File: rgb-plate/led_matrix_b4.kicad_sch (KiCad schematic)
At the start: 32 parts

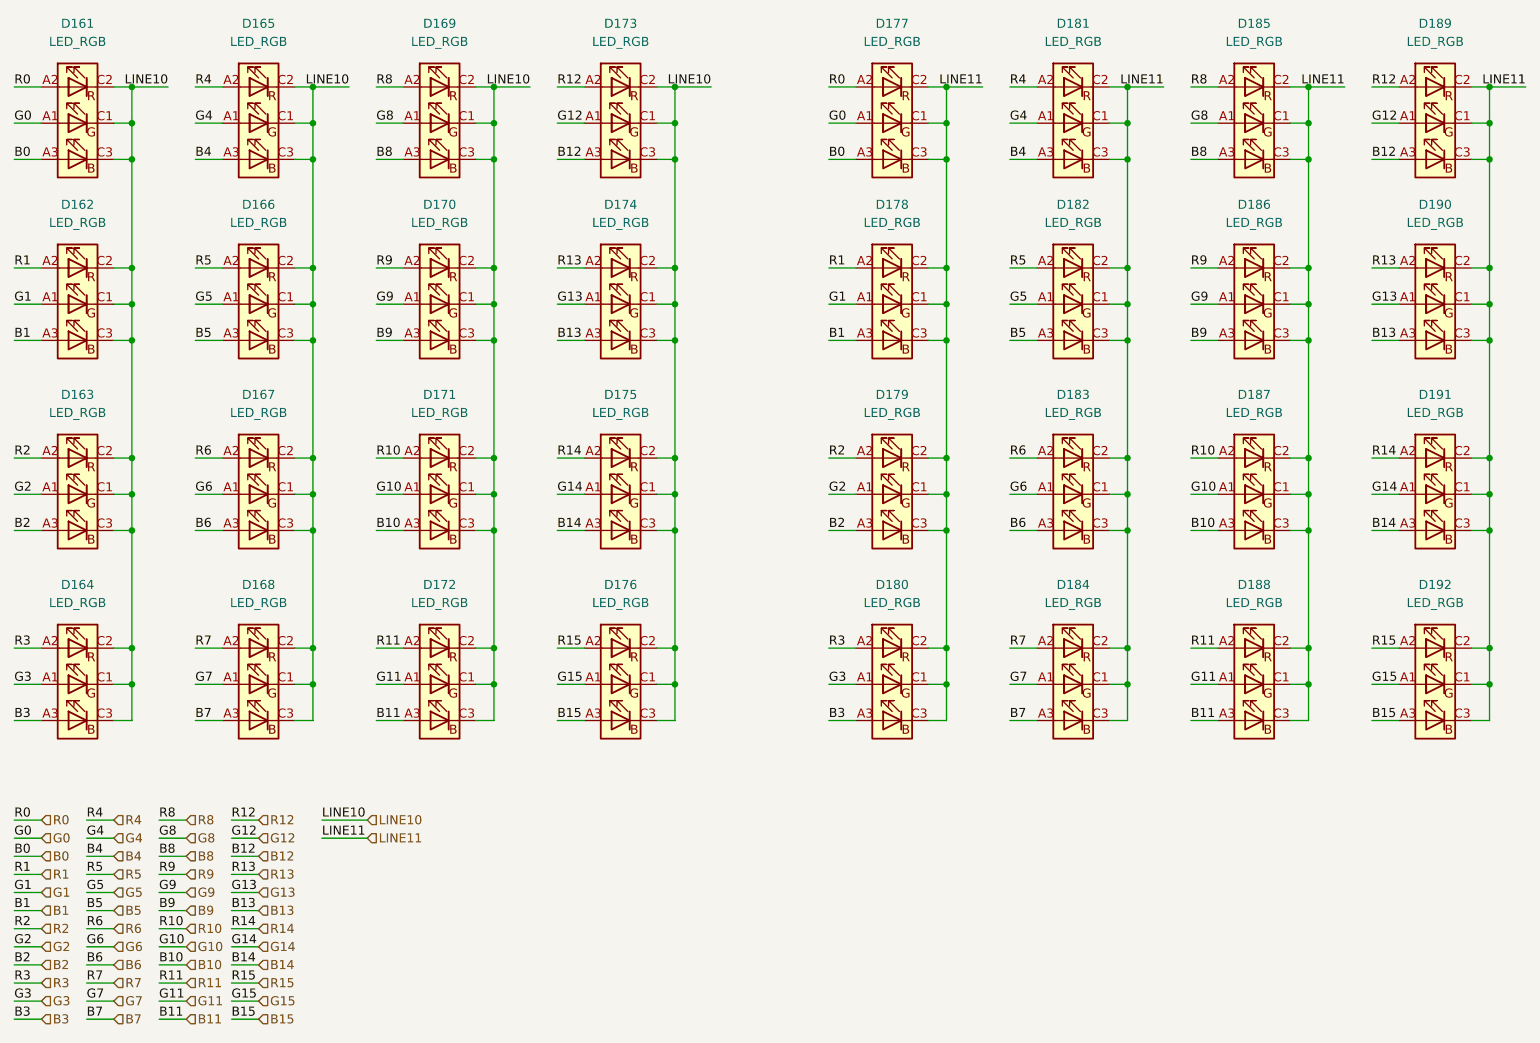
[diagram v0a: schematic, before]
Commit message: initial layout on single board, may need to split up
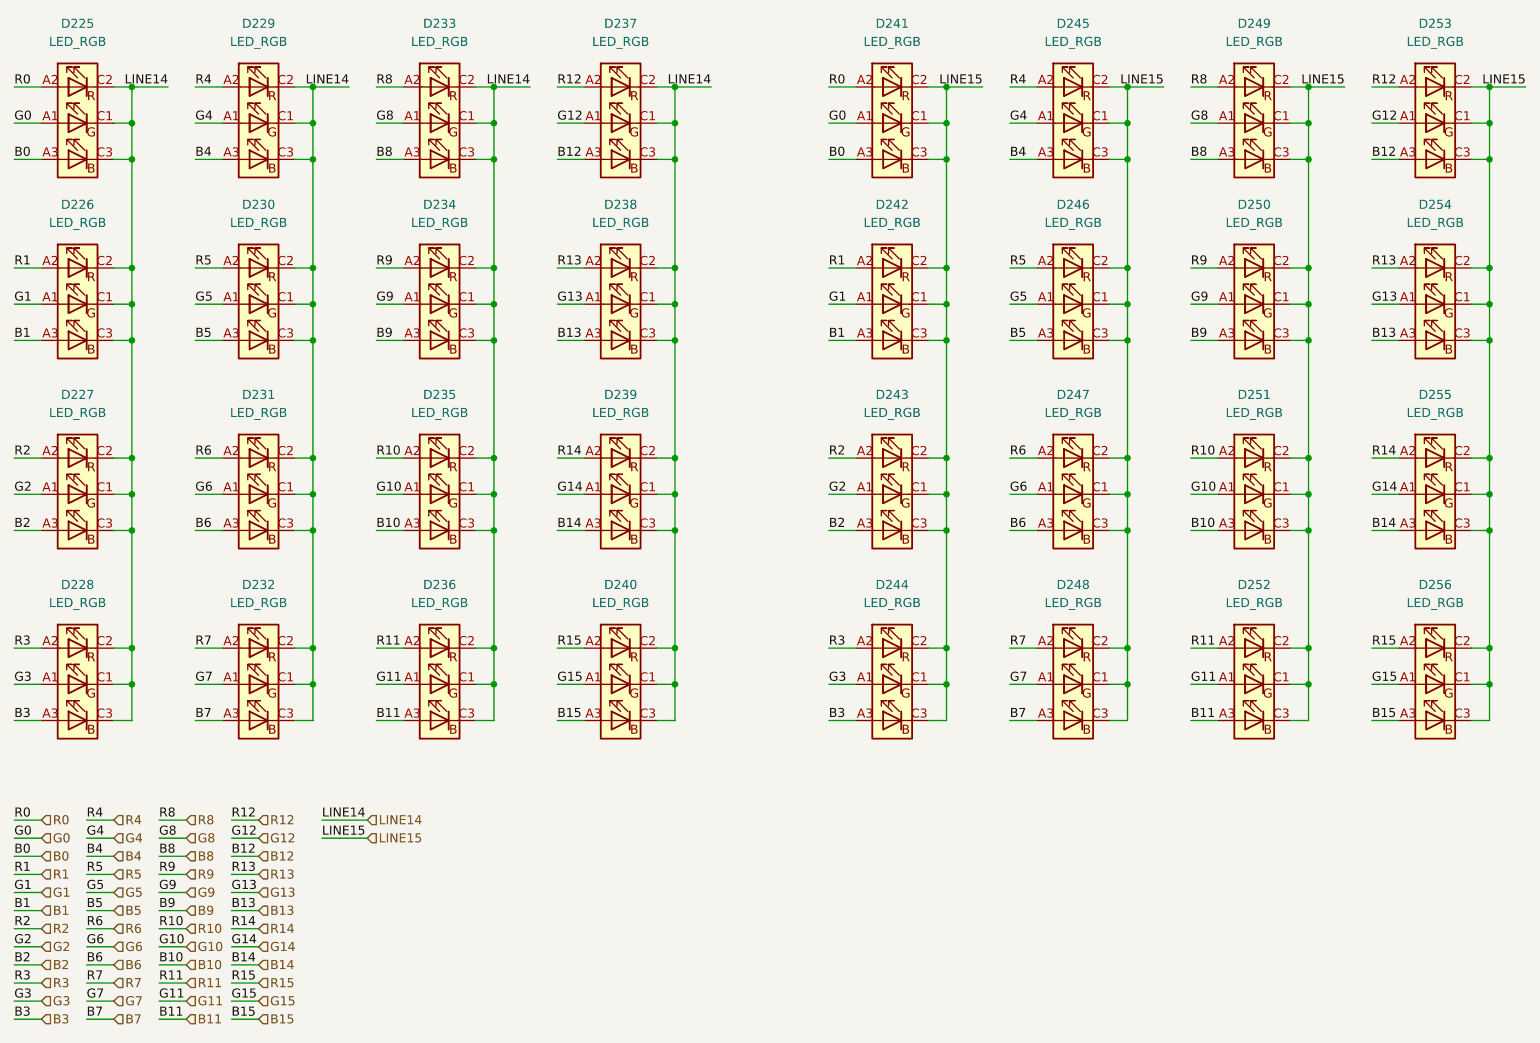
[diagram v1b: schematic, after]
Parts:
- removed D161, D162, D163, D164, D165, D166, D167, D168, D169, D170, D171, D172, D173, D174, D175, D176, D177, D178, D179, D180, D181, D182, D183, D184, D185, D186, D187, D188, D189, D190, D191, D192: LED_RGB, LRTBGVSR-4U4V-JW+8A8B-D8-3S4U-7Z:LRTBGVSR4U4VJW8A8BD83S4U7Z, symbol LRTBGVSR-4U4V-JW+8A8B-D8-3S4U-:LED_RGB
- added D225, D226, D227, D228, D229, D230, D231, D232, D233, D234, D235, D236, D237, D238, D239, D240, D241, D242, D243, D244, D245, D246, D247, D248, D249, D250, D251, D252, D253, D254, D255, D256: LED_RGB, LRTBGVSR-4U4V-JW+8A8B-D8-3S4U-7Z:LRTBGVSR4U4VJW8A8BD83S4U7Z, symbol LRTBGVSR-4U4V-JW+8A8B-D8-3S4U-:LED_RGB
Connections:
- net B0: now also D225.A3 (BA), D241.A3 (BA)
- net B1: now also D226.A3 (BA), D242.A3 (BA)
- net B10: now also D235.A3 (BA), D251.A3 (BA)
- net B11: now also D236.A3 (BA), D252.A3 (BA)
- net B12: now also D237.A3 (BA), D253.A3 (BA)
- net B13: now also D238.A3 (BA), D254.A3 (BA)
- net B14: now also D239.A3 (BA), D255.A3 (BA)
- net B15: now also D240.A3 (BA), D256.A3 (BA)
- net B2: now also D227.A3 (BA), D243.A3 (BA)
- net B3: now also D228.A3 (BA), D244.A3 (BA)
- net B4: now also D229.A3 (BA), D245.A3 (BA)
- net B5: now also D230.A3 (BA), D246.A3 (BA)
- net B6: now also D231.A3 (BA), D247.A3 (BA)
- net B7: now also D232.A3 (BA), D248.A3 (BA)
- net B8: now also D233.A3 (BA), D249.A3 (BA)
- net B9: now also D234.A3 (BA), D250.A3 (BA)
- net G0: now also D225.A1 (GA), D241.A1 (GA)
- net G1: now also D226.A1 (GA), D242.A1 (GA)
- net G10: now also D235.A1 (GA), D251.A1 (GA)
- net G11: now also D236.A1 (GA), D252.A1 (GA)
- net G12: now also D237.A1 (GA), D253.A1 (GA)
- net G13: now also D238.A1 (GA), D254.A1 (GA)
- net G14: now also D239.A1 (GA), D255.A1 (GA)
- net G15: now also D240.A1 (GA), D256.A1 (GA)
- net G2: now also D227.A1 (GA), D243.A1 (GA)
- net G3: now also D228.A1 (GA), D244.A1 (GA)
- net G4: now also D229.A1 (GA), D245.A1 (GA)
- net G5: now also D230.A1 (GA), D246.A1 (GA)
- net G6: now also D231.A1 (GA), D247.A1 (GA)
- net G7: now also D232.A1 (GA), D248.A1 (GA)
- net G8: now also D233.A1 (GA), D249.A1 (GA)
- net G9: now also D234.A1 (GA), D250.A1 (GA)
- net R0: now also D225.A2 (RA), D241.A2 (RA)
- net R1: now also D226.A2 (RA), D242.A2 (RA)
- net R10: now also D235.A2 (RA), D251.A2 (RA)
- net R11: now also D236.A2 (RA), D252.A2 (RA)
- net R12: now also D237.A2 (RA), D253.A2 (RA)
- net R13: now also D238.A2 (RA), D254.A2 (RA)
- net R14: now also D239.A2 (RA), D255.A2 (RA)
- net R15: now also D240.A2 (RA), D256.A2 (RA)
- net R2: now also D227.A2 (RA), D243.A2 (RA)
- net R3: now also D228.A2 (RA), D244.A2 (RA)
- net R4: now also D229.A2 (RA), D245.A2 (RA)
- net R5: now also D230.A2 (RA), D246.A2 (RA)
- net R6: now also D231.A2 (RA), D247.A2 (RA)
- net R7: now also D232.A2 (RA), D248.A2 (RA)
- net R8: now also D233.A2 (RA), D249.A2 (RA)
- net R9: now also D234.A2 (RA), D250.A2 (RA)
- new net LINE14: D225.C1 (GK), D225.C2 (RK), D225.C3 (BK), D226.C1 (GK), D226.C2 (RK), D226.C3 (BK), D227.C1 (GK), D227.C2 (RK), D227.C3 (BK), D228.C1 (GK), D228.C2 (RK), D228.C3 (BK), D229.C1 (GK), D229.C2 (RK), D229.C3 (BK), D230.C1 (GK), D230.C2 (RK), D230.C3 (BK), D231.C1 (GK), D231.C2 (RK), D231.C3 (BK), D232.C1 (GK), D232.C2 (RK), D232.C3 (BK), D233.C1 (GK), D233.C2 (RK), D233.C3 (BK), D234.C1 (GK), D234.C2 (RK), D234.C3 (BK), D235.C1 (GK), D235.C2 (RK), D235.C3 (BK), D236.C1 (GK), D236.C2 (RK), D236.C3 (BK), D237.C1 (GK), D237.C2 (RK), D237.C3 (BK), D238.C1 (GK), D238.C2 (RK), D238.C3 (BK), D239.C1 (GK), D239.C2 (RK), D239.C3 (BK), D240.C1 (GK), D240.C2 (RK), D240.C3 (BK)
- new net LINE15: D241.C1 (GK), D241.C2 (RK), D241.C3 (BK), D242.C1 (GK), D242.C2 (RK), D242.C3 (BK), D243.C1 (GK), D243.C2 (RK), D243.C3 (BK), D244.C1 (GK), D244.C2 (RK), D244.C3 (BK), D245.C1 (GK), D245.C2 (RK), D245.C3 (BK), D246.C1 (GK), D246.C2 (RK), D246.C3 (BK), D247.C1 (GK), D247.C2 (RK), D247.C3 (BK), D248.C1 (GK), D248.C2 (RK), D248.C3 (BK), D249.C1 (GK), D249.C2 (RK), D249.C3 (BK), D250.C1 (GK), D250.C2 (RK), D250.C3 (BK), D251.C1 (GK), D251.C2 (RK), D251.C3 (BK), D252.C1 (GK), D252.C2 (RK), D252.C3 (BK), D253.C1 (GK), D253.C2 (RK), D253.C3 (BK), D254.C1 (GK), D254.C2 (RK), D254.C3 (BK), D255.C1 (GK), D255.C2 (RK), D255.C3 (BK), D256.C1 (GK), D256.C2 (RK), D256.C3 (BK)
